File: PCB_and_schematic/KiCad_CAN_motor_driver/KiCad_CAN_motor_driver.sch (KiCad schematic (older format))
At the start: 67 parts, among them J1 SWDIO, J2 UART, J3 POWER IN 24V, J4 MOTOR OUT, J5 CAN, J6 PWM_IN, Q1 BTN8982TA, Q2 BTN8982TA, U1 SN65HVD232, U2 LMR50410, U3 STM32F103C8Tx

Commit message: PCB and schematic rev 1.1
+ revision 1.1 of schematic and PCB
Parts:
- removed TP5: DIR, TestPoint:TestPoint_THTPad_D1.0mm_Drill0.5mm, symbol Connector:TestPoint
- removed TP6: PWM IN, TestPoint:TestPoint_THTPad_D1.0mm_Drill0.5mm, symbol Connector:TestPoint
- added C10, C23: 10nF, Capacitor_SMD:C_0805_2012Metric, symbol Device:C_Small
- added C25: 100nF, Capacitor_SMD:C_1206_3216Metric, symbol Device:C_Small
- added D2: SD24_SOD323, Diode_SMD:D_SOD-323, symbol Diode:SD24_SOD323
- added FB1: Ferrite_Bead, Inductor_SMD:L_1206_3216Metric, symbol Device:Ferrite_Bead_Small
- added R1: 10R, Resistor_SMD:R_0805_2012Metric, symbol Device:R_Small
- added R11, R20: 33k, Resistor_SMD:R_0805_2012Metric, symbol Device:R_Small
- C11, C2, C3, C6, C7, C9: footprint Capacitor_SMD:C_1206_3216Metric_Pad1.33x1.80mm_HandSolder -> Capacitor_SMD:C_0805_2012Metric
- C12: renamed from C10; footprint Capacitor_SMD:C_1206_3216Metric_Pad1.33x1.80mm_HandSolder -> Capacitor_SMD:C_0805_2012Metric
- C15: renamed from C16; footprint Capacitor_SMD:C_1206_3216Metric_Pad1.33x1.80mm_HandSolder -> Capacitor_SMD:C_0805_2012Metric
- C16: renamed from C17; footprint Capacitor_SMD:C_1206_3216Metric_Pad1.33x1.80mm_HandSolder -> Capacitor_SMD:C_0805_2012Metric
- C19: renamed from C18; footprint Capacitor_SMD:C_1206_3216Metric_Pad1.33x1.80mm_HandSolder -> Capacitor_SMD:C_0805_2012Metric
- C20: renamed from C19; footprint Capacitor_SMD:C_1206_3216Metric_Pad1.33x1.80mm_HandSolder -> Capacitor_SMD:C_0805_2012Metric
- C21: renamed from C20; footprint Capacitor_SMD:C_1206_3216Metric_Pad1.33x1.80mm_HandSolder -> Capacitor_SMD:C_0805_2012Metric
- C22: renamed from C21; footprint Capacitor_SMD:C_1206_3216Metric_Pad1.33x1.80mm_HandSolder -> Capacitor_SMD:C_0805_2012Metric
- C4: renamed from C5; footprint Capacitor_SMD:C_1206_3216Metric_Pad1.33x1.80mm_HandSolder -> Capacitor_SMD:C_0805_2012Metric
- C5: renamed from C4; footprint Capacitor_SMD:C_1206_3216Metric_Pad1.33x1.80mm_HandSolder -> Capacitor_SMD:C_0805_2012Metric
- D5: renamed from D4; footprint LED_SMD:LED_1206_3216Metric_Castellated -> LED_SMD:LED_0805_2012Metric_Castellated
- J4: renamed from J3; footprint WK_lib:PowerPad_2x_3mm -> WK_lib:ScrewTerminal_2_P5.08mm
- J5: renamed from J4; footprint WK_lib:PowerPad_2x_3mm -> WK_lib:ScrewTerminal_2_P5.08mm
- J6: renamed from J5; footprint WK_lib:PowerPad_2x_3mm -> WK_lib:ScrewTerminal_2_P5.08mm
- R10, R9: footprint Resistor_SMD:R_1206_3216Metric_Pad1.30x1.75mm_HandSolder -> Resistor_SMD:R_0805_2012Metric
- R12: renamed from R8; footprint Resistor_SMD:R_1206_3216Metric_Pad1.30x1.75mm_HandSolder -> Resistor_SMD:R_0805_2012Metric
- R13: renamed from R12; footprint Resistor_SMD:R_1206_3216Metric_Pad1.30x1.75mm_HandSolder -> Resistor_SMD:R_0805_2012Metric
- R14: renamed from R13; value 1.5k -> 1.1k; footprint Resistor_SMD:R_1206_3216Metric_Pad1.30x1.75mm_HandSolder -> Resistor_SMD:R_0805_2012Metric
- R15: renamed from R11; footprint Resistor_SMD:R_1206_3216Metric_Pad1.30x1.75mm_HandSolder -> Resistor_SMD:R_0805_2012Metric
- R16: renamed from R14; footprint Resistor_SMD:R_1206_3216Metric_Pad1.30x1.75mm_HandSolder -> Resistor_SMD:R_0805_2012Metric
- R17: renamed from R15; footprint Resistor_SMD:R_1206_3216Metric_Pad1.30x1.75mm_HandSolder -> Resistor_SMD:R_0805_2012Metric
- R18: renamed from R16; footprint Resistor_SMD:R_1206_3216Metric_Pad1.30x1.75mm_HandSolder -> Resistor_SMD:R_0805_2012Metric
- R19: renamed from R17; footprint Resistor_SMD:R_1206_3216Metric_Pad1.30x1.75mm_HandSolder -> Resistor_SMD:R_0805_2012Metric
- R2: renamed from R1; footprint Resistor_SMD:R_1206_3216Metric_Pad1.30x1.75mm_HandSolder -> Resistor_SMD:R_0805_2012Metric
- R3: renamed from R2; footprint Resistor_SMD:R_1206_3216Metric_Pad1.30x1.75mm_HandSolder -> Resistor_SMD:R_0805_2012Metric
- R4: renamed from R3; footprint Resistor_SMD:R_1206_3216Metric_Pad1.30x1.75mm_HandSolder -> Resistor_SMD:R_0805_2012Metric
- R5: renamed from R4; footprint Resistor_SMD:R_1206_3216Metric_Pad1.30x1.75mm_HandSolder -> Resistor_SMD:R_0805_2012Metric
- R6: renamed from R5; footprint Resistor_SMD:R_1206_3216Metric_Pad1.30x1.75mm_HandSolder -> Resistor_SMD:R_0805_2012Metric
- R7: renamed from R6; footprint Resistor_SMD:R_1206_3216Metric_Pad1.30x1.75mm_HandSolder -> Resistor_SMD:R_0805_2012Metric
- R8: renamed from R7; footprint Resistor_SMD:R_1206_3216Metric_Pad1.30x1.75mm_HandSolder -> Resistor_SMD:R_0805_2012Metric
- TH2: footprint Resistor_THT:R_Axial_DIN0414_L11.9mm_D4.5mm_P5.08mm_Vertical -> Connector_PinHeader_2.54mm:PinHeader_1x02_P2.54mm_Vertical
- renumbered C12 to C13, C13 to C14, C14 to C17, C15 to C18, D2 to D3, D3 to D4, FB1 to FB2, J6 to J3, JP3 to JP1, JP1 to JP2, JP2 to JP3, TP4 to TP5
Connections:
- net +24V: now also J4.1 (Pin_1); no longer J4.2 (Pin_2)
- net +3V3: now also FB1.1; no longer C7.1, C8.1, L1.2, R6.1
- net CAN_H: now also J6.1 (Pin_1); no longer J6.2 (Pin_2)
- net CAN_L: now also J6.2 (Pin_2); no longer J6.1 (Pin_1)
- net GND: now also J4.2 (Pin_2), C10.2, C23.2, D2.2 (A2); no longer J4.1 (Pin_1)
- net I_SENSE_1: now also C10.1, R11.1; no longer C12.1, Q1.6 (IS), R12.1
- net I_SENSE_2: now also C23.1, R20.2; no longer C22.1, Q2.6 (IS), R19.1
- net MOT_A: now also C25.1
- net MOT_B: now also C25.2
- net at C1.1, C2.1, U2.4 (EN)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: now also D2.1 (A1), R1.2; no longer D1.1 (K)
- new net: C12.1, Q1.6 (IS), R11.2, R12.1
- new net: C7.1, C8.1, FB1.2, L1.2, R6.1
- new net: C22.1, Q2.6 (IS), R19.1, R20.1
- new net: D1.1 (K), R1.1
- no-connect marks 0 -> 21
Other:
- moved on the sheet: C1, C11, C12, C13, C14, C15, C16, C17, C18, C19, C2, C20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

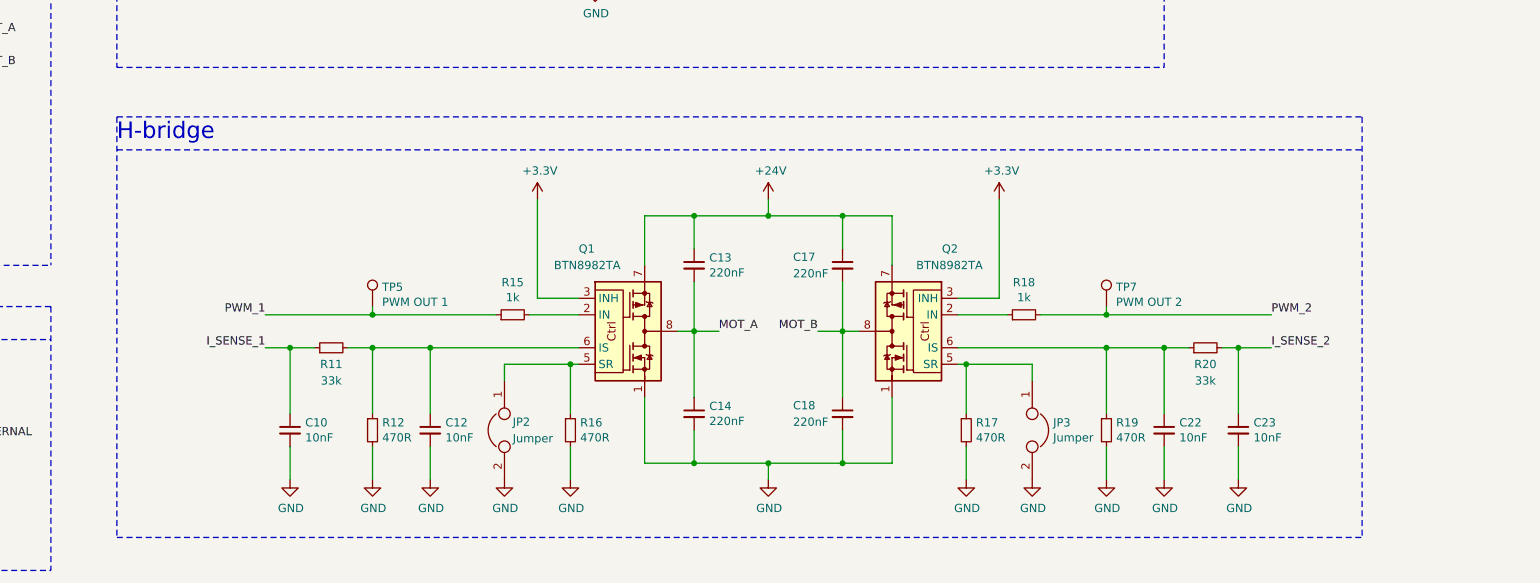
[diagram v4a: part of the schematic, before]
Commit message: Added back-emf diodes, fixed reading errors
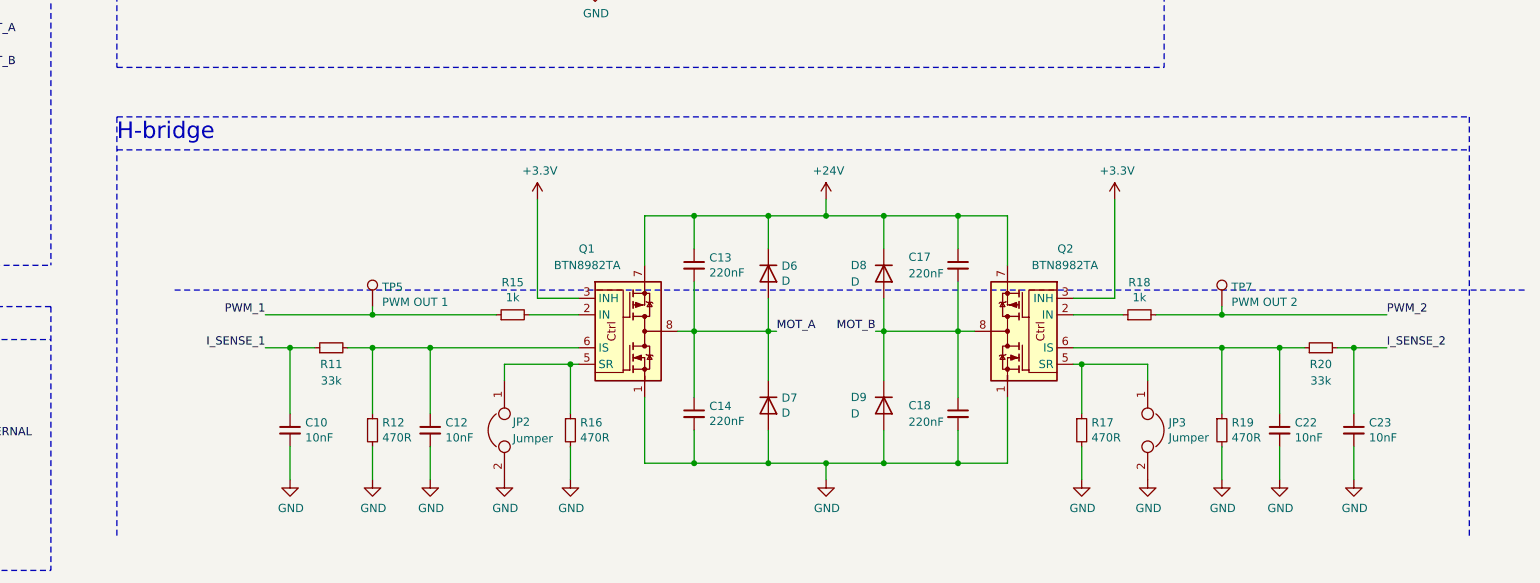
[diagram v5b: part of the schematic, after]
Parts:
- added D6, D7, D8, D9: D, Diode_SMD:D_PowerDI-123, symbol Device:D
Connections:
- net +24V: now also D6.1 (K), D8.1 (K)
- net GND: now also D7.2 (A), D9.2 (A)
- net MOT_A: now also D6.2 (A), D7.1 (K)
- net MOT_B: now also D8.2 (A), D9.1 (K)
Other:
- moved on the sheet: C17, C18, C22, C23, JP3, Q2, R17, R18, R19, R20, TP7
